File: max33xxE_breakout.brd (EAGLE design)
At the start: 48.3 x 15.2 mm, 30 parts

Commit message: route the VCC solder jumpers
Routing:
- net VCC_SHIFT3: track 6.39 -> 14.0 mm
- net VCC_SHIFT1: track 4.05 -> 11.7 mm
- net VCC_SHIFT2: track 6.04 -> 13.6 mm
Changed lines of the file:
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@@
 <attribute name="VALUE" x="39.9425" y="10.325" size="1.016" layer="27" rot="R270"/>
 </element>
-<element name="SJ1" library="SparkFun-Passives" package="SJ_2S-TRACE" value="SOLDERJUMPERTRACE" x="11.43" y="10.16"/>
-<element name="SJ2" library="SparkFun-Passives" package="SJ_2S-TRACE" value="SOLDERJUMPERTRACE" x="24.13" y="5.08"/>
-<element name="SJ3" library="SparkFun-Passives" package="SJ_2S-TRACE" value="SOLDERJUMPERTRACE" x="36.83" y="5.08"/>
-<element name="SJ4" library="SparkFun-Passives" package="SJ_2S-TRACE" value="SOLDERJUMPERTRACE" x="36.83" y="10.16"/>
-<element name="SJ5" library="SparkFun-Passives" package="SJ_2S-TRACE" value="SOLDERJUMPERTRACE" x="24.13" y="10.16"/>
-<element name="SJ6" library="SparkFun-Passives" package="SJ_2S-TRACE" value="SOLDERJUMPERTRACE" x="11.43" y="5.08"/>
+<element name="SJ1" library="SparkFun-Passives" package="SJ_2S-TRACE" value="SOLDERJUMPERTRACE" x="11.43" y="10.16" smashed="yes"/>
+<element name="SJ2" library="SparkFun-Passives" package="SJ_2S-TRACE" value="SOLDERJUMPERTRACE" x="24.13" y="5.08" smashed="yes"/>
+<element name="SJ3" library="SparkFun-Passives" package="SJ_2S-TRACE" value="SOLDERJUMPERTRACE" x="36.83" y="5.08" smashed="yes"/>
+<element name="SJ4" library="SparkFun-Passives" package="SJ_2S-TRACE" value="SOLDERJUMPERTRACE" x="36.83" y="10.16" smashed="yes"/>
+<element name="SJ5" library="SparkFun-Passives" package="SJ_2S-TRACE" value="SOLDERJUMPERTRACE" x="24.13" y="10.16" smashed="yes"/>
+<element name="SJ6" library="SparkFun-Passives" package="SJ_2S-TRACE" value="SOLDERJUMPERTRACE" x="11.43" y="5.08" smashed="yes"/>
 </elements>
 <signals>
@@
 <wire x1="3.3528" y1="10.3632" x2="3.4925" y2="10.4" width="0.254" layer="1"/>
 <wire x1="1.3716" y1="10.2108" x2="1.27" y2="10.16" width="0.254" layer="1"/>
-<wire x1="5.035" y1="10.5378" x2="10.922" y2="10.16" width="0" layer="19" extent="1-1"/>
+<wire x1="10.922" y1="10.16" x2="10.63625" y2="10.16" width="0.254" layer="1"/>
+<wire x1="10.63625" y1="10.16" x2="9.68375" y2="9.2075" width="0.254" layer="1"/>
+<wire x1="9.68375" y1="9.2075" x2="5.0546" y2="9.2075" width="0.254" layer="1"/>
+<wire x1="5.0546" y1="9.2075" x2="5.0546" y2="10.4928" width="0.254" layer="1"/>
+<wire x1="5.0546" y1="10.4928" x2="5.035" y2="10.5378" width="0.254" layer="1"/>
 </signal>
 <signal name="VL_SHIFT1">
@@
 <wire x1="16.1544" y1="4.8768" x2="16.1925" y2="4.84" width="0.254" layer="1"/>
 <wire x1="14.0208" y1="5.0292" x2="13.97" y2="5.08" width="0.254" layer="1"/>
+<wire x1="13.97" y1="5.08" x2="11.938" y2="5.08" width="0.254" layer="1"/>
 <wire x1="17.735" y1="4.7022" x2="23.622" y2="5.08" width="0" layer="19" extent="1-1"/>
-<wire x1="13.97" y1="5.08" x2="11.938" y2="5.08" width="0.254" layer="1"/>
 </signal>
 <signal name="VCC_SHIFT2">
@@
 <wire x1="16.1544" y1="10.3632" x2="16.1925" y2="10.4" width="0.254" layer="1"/>
 <wire x1="14.0208" y1="10.2108" x2="13.97" y2="10.16" width="0.254" layer="1"/>
-<wire x1="17.735" y1="10.5378" x2="23.622" y2="10.16" width="0" layer="19" extent="1-1"/>
 <wire x1="13.97" y1="10.16" x2="11.938" y2="10.16" width="0.254" layer="1"/>
+<wire x1="23.622" y1="10.16" x2="23.33625" y2="10.16" width="0.254" layer="1"/>
+<wire x1="23.33625" y1="10.16" x2="22.38375" y2="9.2075" width="0.254" layer="1"/>
+<wire x1="22.38375" y1="9.2075" x2="17.7546" y2="9.2075" width="0.254" layer="1"/>
+<wire x1="17.7546" y1="9.2075" x2="17.7546" y2="10.4674" width="0.254" layer="1"/>
+<wire x1="17.7546" y1="10.4674" x2="17.735" y2="10.5378" width="0.254" layer="1"/>
 </signal>
 <signal name="IOVCC4_SHIFT3">
@@
 <wire x1="28.8036" y1="4.8768" x2="28.8925" y2="4.84" width="0.254" layer="1"/>
 <wire x1="26.67" y1="5.0292" x2="26.67" y2="5.08" width="0.254" layer="1"/>
+<wire x1="26.67" y1="5.08" x2="24.638" y2="5.08" width="0.254" layer="1"/>
 <wire x1="30.435" y1="4.7022" x2="36.322" y2="5.08" width="0" layer="19" extent="1-1"/>
-<wire x1="26.67" y1="5.08" x2="24.638" y2="5.08" width="0.254" layer="1"/>
 </signal>
 <signal name="VCC_SHIFT3">
@@
 <wire x1="28.956" y1="10.5156" x2="28.8925" y2="10.4" width="0.254" layer="1"/>
 <wire x1="24.638" y1="10.3632" x2="24.638" y2="10.16" width="0.254" layer="1"/>
-<wire x1="30.435" y1="10.5378" x2="36.322" y2="10.16" width="0" layer="19" extent="1-1"/>
 <wire x1="24.638" y1="10.16" x2="26.67" y2="10.16" width="0.254" layer="1"/>
 <wire x1="26.67" y1="10.16" x2="26.797" y2="10.16" width="0.254" layer="1"/>
@@
 <wire x1="26.797" y1="10.4394" x2="28.8925" y2="10.4394" width="0.254" layer="1"/>
 <wire x1="28.8925" y1="10.4394" x2="28.8925" y2="10.4" width="0.254" layer="1"/>
+<wire x1="36.322" y1="10.16" x2="36.03625" y2="10.16" width="0.254" layer="1"/>
+<wire x1="36.03625" y1="10.16" x2="35.08375" y2="9.2075" width="0.254" layer="1"/>
+<wire x1="35.08375" y1="9.2075" x2="30.4546" y2="9.2075" width="0.254" layer="1"/>
+<wire x1="30.4546" y1="9.2075" x2="30.4546" y2="10.5182" width="0.254" layer="1"/>
+<wire x1="30.4546" y1="10.5182" x2="30.435" y2="10.5378" width="0.254" layer="1"/>
 </signal>
 <signal name="IOVCC4_SHIFT4">

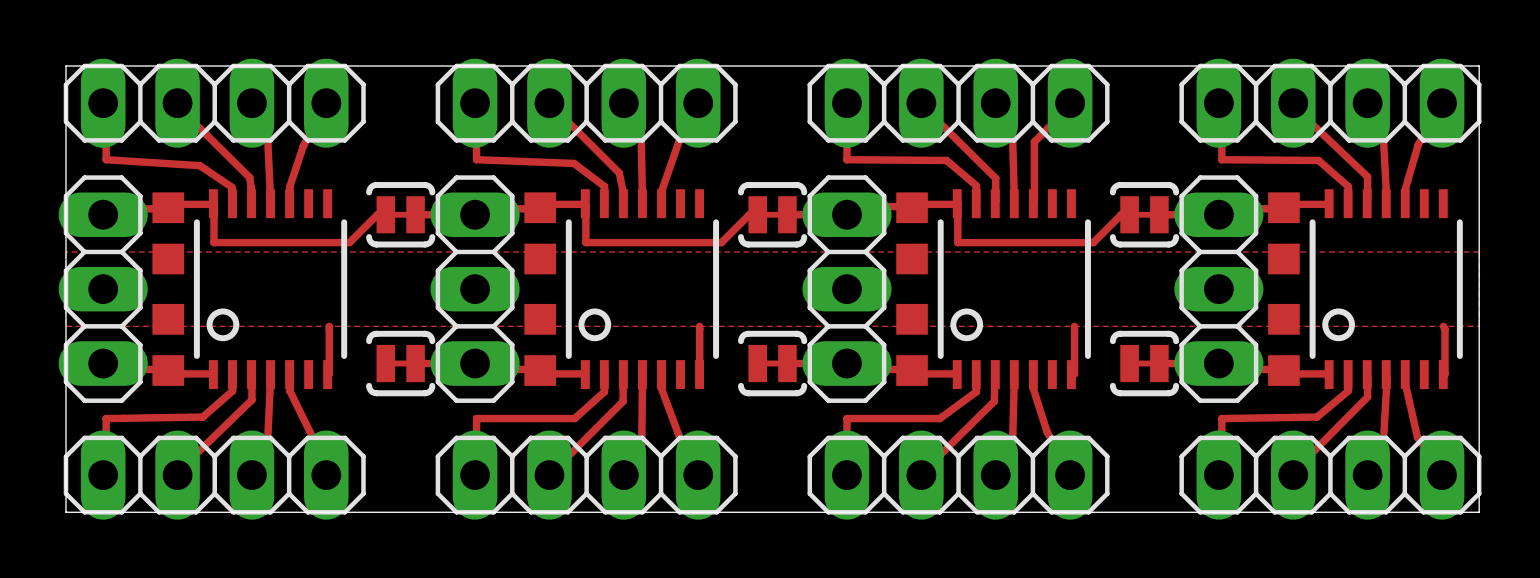
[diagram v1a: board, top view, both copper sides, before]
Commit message: add vias to route the VL solder jumpers from bottom
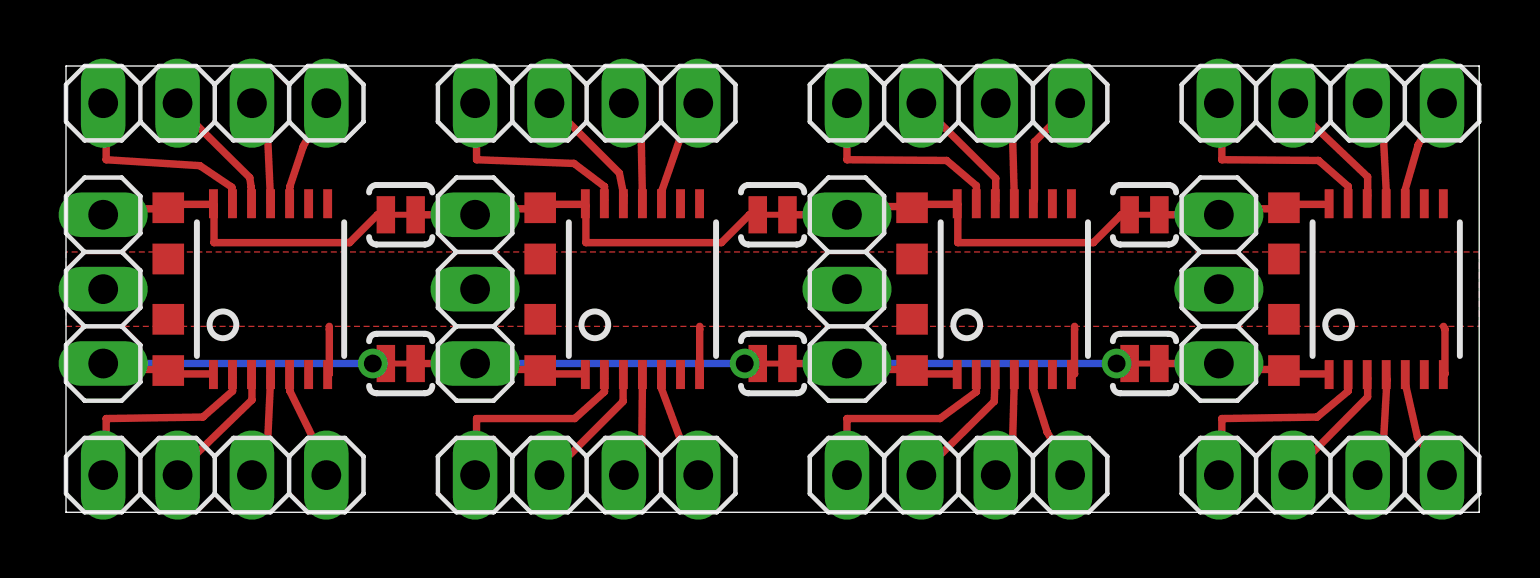
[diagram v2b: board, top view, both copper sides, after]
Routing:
- net VL_SHIFT3: track 6.08 -> 15.7 mm, vias 0 -> 1
- net VL_SHIFT1: track 4.05 -> 13.7 mm, vias 0 -> 1
- net VL_SHIFT2: track 6.04 -> 15.7 mm, vias 0 -> 1
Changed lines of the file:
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@@
 <setting verticaltext="up"/>
 </settings>
-<grid distance="1" unitdist="mil" unit="mil" style="lines" multiple="1" display="yes" altdistance="0.025" altunitdist="inch" altunit="inch"/>
+<grid distance="12.5" unitdist="mil" unit="mil" style="lines" multiple="1" display="yes" altdistance="0.025" altunitdist="inch" altunit="inch"/>
 <layers>
 <layer number="1" name="Top" color="4" fill="1" visible="yes" active="yes"/>
@@
 <wire x1="3.3528" y1="4.8768" x2="3.4925" y2="4.84" width="0.254" layer="1"/>
 <wire x1="1.3716" y1="5.0292" x2="1.27" y2="5.08" width="0.254" layer="1"/>
-<wire x1="5.035" y1="4.7022" x2="10.922" y2="5.08" width="0" layer="19" extent="1-1"/>
+<via x="10.4775" y="5.08" extent="1-16" drill="0.6096"/>
+<wire x1="10.4775" y1="5.08" x2="1.27" y2="5.08" width="0.254" layer="16"/>
+<wire x1="10.4775" y1="5.08" x2="10.922" y2="5.08" width="0.254" layer="1"/>
 </signal>
 <signal name="IOVL2_SHIFT1">
@@
 <wire x1="14.0208" y1="5.0292" x2="13.97" y2="5.08" width="0.254" layer="1"/>
 <wire x1="13.97" y1="5.08" x2="11.938" y2="5.08" width="0.254" layer="1"/>
-<wire x1="17.735" y1="4.7022" x2="23.622" y2="5.08" width="0" layer="19" extent="1-1"/>
+<via x="23.1775" y="5.08" extent="1-16" drill="0.6096"/>
+<wire x1="23.1775" y1="5.08" x2="13.97" y2="5.08" width="0.254" layer="16"/>
+<wire x1="23.1775" y1="5.08" x2="23.622" y2="5.08" width="0.254" layer="1"/>
 </signal>
 <signal name="VCC_SHIFT2">
@@
 <wire x1="26.67" y1="5.0292" x2="26.67" y2="5.08" width="0.254" layer="1"/>
 <wire x1="26.67" y1="5.08" x2="24.638" y2="5.08" width="0.254" layer="1"/>
-<wire x1="30.435" y1="4.7022" x2="36.322" y2="5.08" width="0" layer="19" extent="1-1"/>
+<via x="35.8775" y="5.08" extent="1-16" drill="0.6096"/>
+<wire x1="35.8775" y1="5.08" x2="26.67" y2="5.08" width="0.254" layer="16"/>
+<wire x1="35.8775" y1="5.08" x2="36.322" y2="5.08" width="0.254" layer="1"/>
 </signal>
 <signal name="VCC_SHIFT3">
